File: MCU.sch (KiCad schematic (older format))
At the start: 4 parts

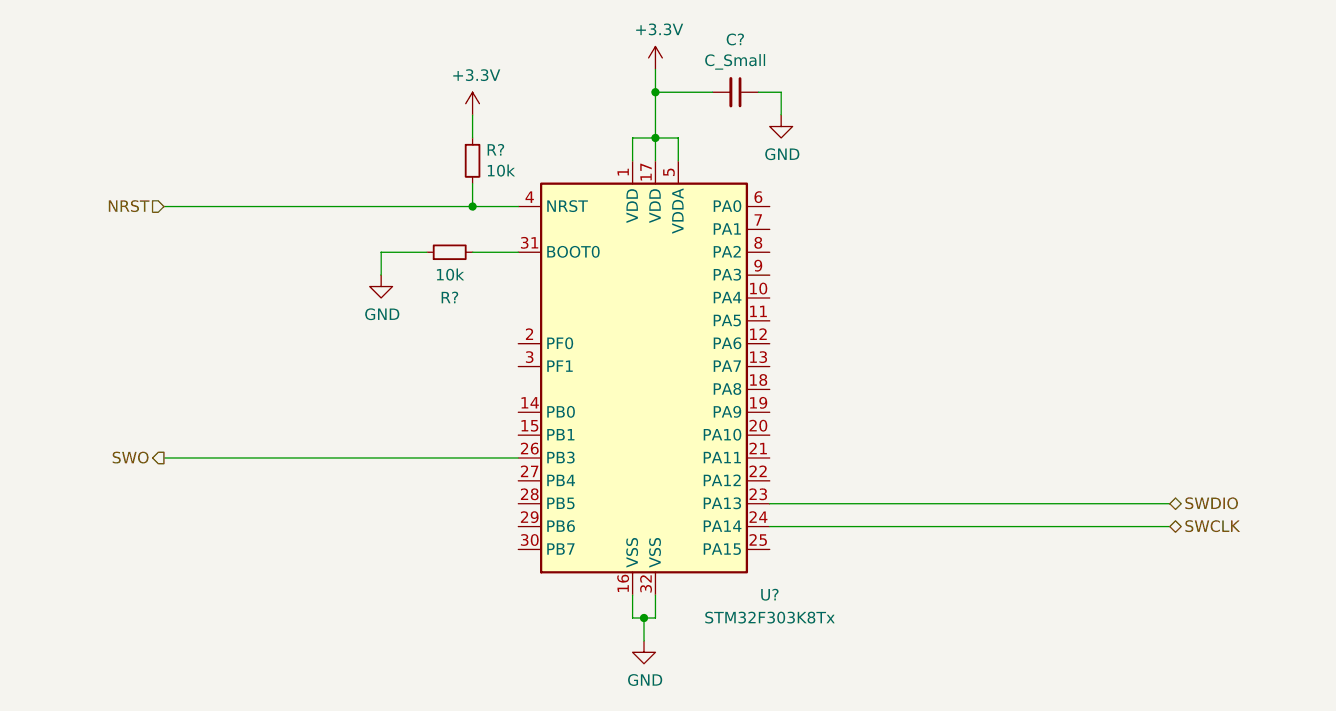
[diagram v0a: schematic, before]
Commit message: デッドタイム挿入回路を削除、マイコンブロック作成
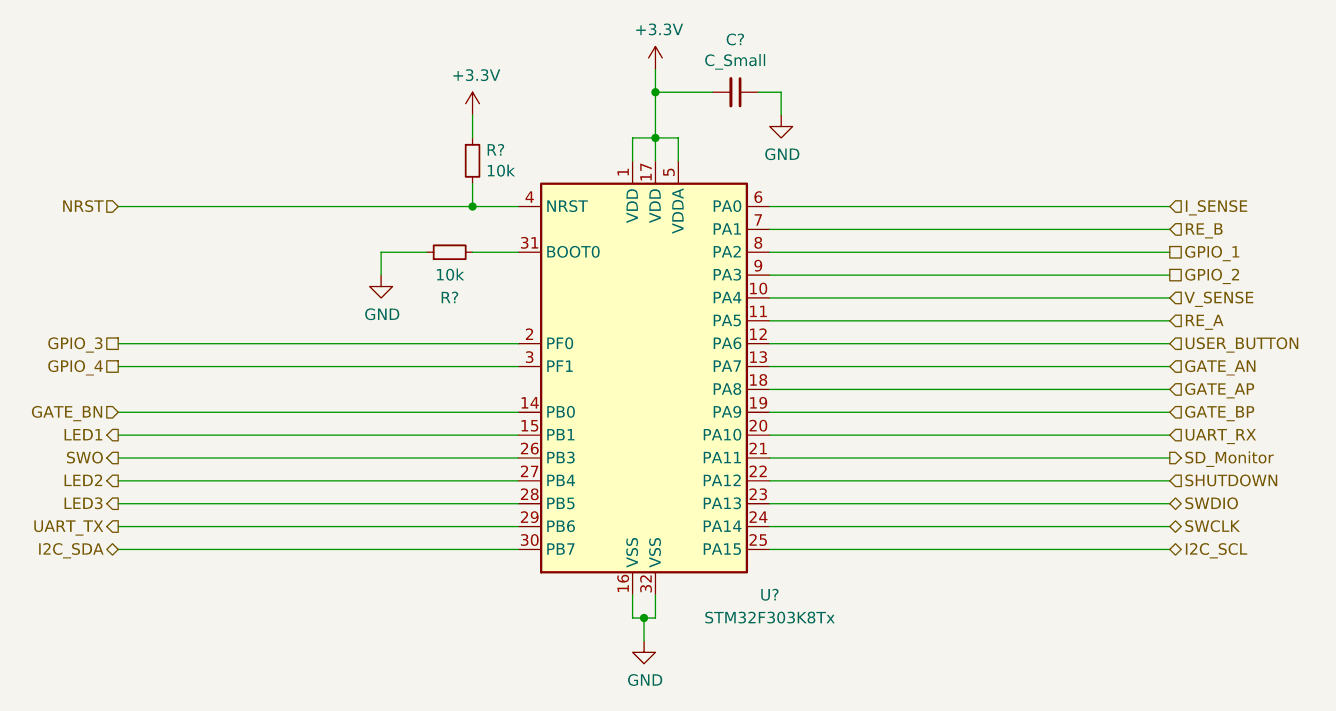
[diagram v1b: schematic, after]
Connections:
- net V_SENSE: now reaches U?.10 (PA4)
- net RE_A: now reaches U?.11 (PA5)
- net USER_BUTTON: now reaches U?.12 (PA6)
- net GATE_AN: now reaches U?.13 (PA7)
- net GATE_BN: now reaches U?.14 (PB0)
- net LED1: now reaches U?.15 (PB1)
- net GATE_AP: now reaches U?.18 (PA8)
- net GATE_BP: now reaches U?.19 (PA9)
- net GPIO_3: now reaches U?.2 (PF0)
- net UART_RX: now reaches U?.20 (PA10)
- net SD_Monitor: now reaches U?.21 (PA11)
- net SHUTDOWN: now reaches U?.22 (PA12)
- net I2C_SCL: now reaches U?.25 (PA15)
- net LED2: now reaches U?.27 (PB4)
- net LED3: now reaches U?.28 (PB5)
- net UART_TX: now reaches U?.29 (PB6)
- net GPIO_4: now reaches U?.3 (PF1)
- net I2C_SDA: now reaches U?.30 (PB7)
- net I_SENSE: now reaches U?.6 (PA0)
- net RE_B: now reaches U?.7 (PA1)
- net GPIO_1: now reaches U?.8 (PA2)
- net GPIO_2: now reaches U?.9 (PA3)
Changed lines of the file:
@@
 Wire Wire Line
 	5000 2750 5000 2850
-Text HLabel 3650 3150 0    50   Input ~ 0
+Text HLabel 3450 3150 0    50   Input ~ 0
 NRST
 Wire Wire Line
-	3650 3150 5000 3150
+	3450 3150 5000 3150
 Connection ~ 5000 3150
 $Comp
@@
 	6300 4550 8050 4550
 Wire Wire Line
-	5200 4250 3650 4250
-Text HLabel 3650 4250 0    50   Output ~ 0
+	5200 4250 3450 4250
+Text HLabel 3450 4250 0    50   Output ~ 0
 SWO
+Text HLabel 8050 3150 2    50   Input ~ 0
+I_SENSE
+Text HLabel 8050 3550 2    50   Input ~ 0
+V_SENSE
+Wire Wire Line
+	6300 3150 8050 3150
+Wire Wire Line
+	8050 3550 6300 3550
+Wire Wire Line
+	6300 3950 8050 3950
+Text HLabel 8050 3950 2    50   Input ~ 0
+GATE_AP
+Text HLabel 8050 3850 2    50   Input ~ 0
+GATE_AN
+Wire Wire Line
+	8050 3850 6300 3850
+Text HLabel 8050 4050 2    50   Input ~ 0
+GATE_BP
+Wire Wire Line
+	8050 4050 6300 4050
+Wire Wire Line
+	5200 4050 3450 4050
+Text HLabel 3450 4050 0    50   Input ~ 0
+GATE_BN
+Text HLabel 3450 4550 0    50   Output ~ 0
+UART_TX
+Wire Wire Line
+	3450 4550 5200 4550
+Text HLabel 8050 4150 2    50   Input ~ 0
+UART_RX
+Wire Wire Line
+	6300 4150 8050 4150
+Wire Wire Line
+	5200 4650 3450 4650
+Text HLabel 3450 4650 0    50   BiDi ~ 0
+I2C_SDA
+Text HLabel 8050 4650 2    50   BiDi ~ 0
+I2C_SCL
+Wire Wire Line
+	8050 4650 6300 4650
+Text HLabel 8050 3650 2    50   Input ~ 0
+RE_A
+Wire Wire Line
+	8050 3650 6300 3650
+Text HLabel 8050 3250 2    50   Input ~ 0
+RE_B
+Wire Wire Line
+	8050 3250 6300 3250
+Text HLabel 3450 4150 0    50   Output ~ 0
+LED1
+Text HLabel 3450 4350 0    50   Output ~ 0
+LED2
+Text HLabel 3450 4450 0    50   Output ~ 0
+LED3
+Wire Wire Line
+	3450 4150 5200 4150
+Wire Wire Line
+	5200 4350 3450 4350
+Wire Wire Line
+	3450 4450 5200 4450
+Text HLabel 8050 3750 2    50   Input ~ 0
+USER_BUTTON
+Wire Wire Line
+	8050 3750 6300 3750
+Text HLabel 8050 4250 2    50   Output ~ 0
+SD_Monitor
+Text HLabel 8050 4350 2    50   Input ~ 0
+SHUTDOWN
+Wire Wire Line
+	6300 4250 8050 4250
+Wire Wire Line
+	6300 4350 8050 4350
+Text HLabel 8050 3350 2    50   UnSpc ~ 0
+GPIO_1
+Text HLabel 8050 3450 2    50   UnSpc ~ 0
+GPIO_2
+Text HLabel 3450 3750 0    50   UnSpc ~ 0
+GPIO_3
+Text HLabel 3450 3850 0    50   UnSpc ~ 0
+GPIO_4
+Wire Wire Line
+	3450 3750 5200 3750
+Wire Wire Line
+	5200 3850 3450 3850
+Wire Wire Line
+	8050 3350 6300 3350
+Wire Wire Line
+	6300 3450 8050 3450
 $EndSCHEMATC

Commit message: 第１版回路図完成
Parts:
- C12: renamed from C?; value C_Small -> 0.1u
- gave numbers to parts that had none: 3
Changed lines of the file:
@@
 encoding utf-8
 Sheet 2 5
-Title ""
+Title "MCU"
 Date ""
 Rev ""
@@
 $EndDescr
 $Comp
-L MCU_ST_STM32F3:STM32F303K8Tx U?
+L MCU_ST_STM32F3:STM32F303K8Tx U4
 U 1 1 5C7B8CAF
 P 5800 3850
-F 0 "U?" H 6300 2850 50  0000 C CNN
+F 0 "U4" H 6300 2850 50  0000 C CNN
 F 1 "STM32F303K8Tx" H 6300 2750 50  0000 C CNN
 F 2 "Package_QFP:LQFP-32_7x7mm_P0.8mm" H 5300 2950 50  0001 R CNN
@@
 $EndComp
 $Comp
-L power:GND #PWR?
+L power:GND #PWR033
 U 1 1 5C94C9F7
 P 5750 5050
-F 0 "#PWR?" H 5750 4800 50  0001 C CNN
+F 0 "#PWR033" H 5750 4800 50  0001 C CNN
 F 1 "GND" H 5755 4877 50  0000 C CNN
 F 2 "" H 5750 5050 50  0001 C CNN
@@
 Connection ~ 5800 2850
 $Comp
-L power:+3.3V #PWR?
+L power:+3.3V #PWR034
 U 1 1 5C94CACA
 P 5800 2550
-F 0 "#PWR?" H 5800 2400 50  0001 C CNN
+F 0 "#PWR034" H 5800 2400 50  0001 C CNN
 F 1 "+3.3V" H 5815 2723 50  0000 C CNN
 F 2 "" H 5800 2550 50  0001 C CNN
@@
 	5800 2550 5800 2650
 $Comp
-L Device:C_Small C?
+L Device:C_Small C12
 U 1 1 5C94CBDE
 P 6150 2650
-F 0 "C?" V 5921 2650 50  0000 C CNN
-F 1 "C_Small" V 6012 2650 50  0000 C CNN
+F 0 "C12" V 5921 2650 50  0000 C CNN
+F 1 "0.1u" V 6012 2650 50  0000 C CNN
 F 2 "" H 6150 2650 50  0001 C CNN
 F 3 "~" H 6150 2650 50  0001 C CNN
@@
 	6350 2650 6350 2750
 $Comp
-L power:GND #PWR?
+L power:GND #PWR035
 U 1 1 5C94CD56
 P 6350 2750
-F 0 "#PWR?" H 6350 2500 50  0001 C CNN
+F 0 "#PWR035" H 6350 2500 50  0001 C CNN
 F 1 "GND" H 6355 2577 50  0000 C CNN
 F 2 "" H 6350 2750 50  0001 C CNN
@@
 $EndComp
 $Comp
-L Device:R_Small R?
+L Device:R_Small R12
 U 1 1 5C94D649
 P 5000 2950
-F 0 "R?" H 5059 2996 50  0000 L CNN
+F 0 "R12" H 5059 2996 50  0000 L CNN
 F 1 "10k" H 5059 2905 50  0000 L CNN
 F 2 "" H 5000 2950 50  0001 C CNN
@@
 	5000 3150 5000 3050
 $Comp
-L power:+3.3V #PWR?
+L power:+3.3V #PWR032
 U 1 1 5C94D8DA
 P 5000 2750
-F 0 "#PWR?" H 5000 2600 50  0001 C CNN
+F 0 "#PWR032" H 5000 2600 50  0001 C CNN
 F 1 "+3.3V" H 5015 2923 50  0000 C CNN
 F 2 "" H 5000 2750 50  0001 C CNN
@@
 Connection ~ 5000 3150
 $Comp
-L Device:R_Small R?
+L Device:R_Small R11
 U 1 1 5C94DBF8
 P 4900 3350
-F 0 "R?" V 4700 3350 50  0000 C CNN
+F 0 "R11" V 4700 3350 50  0000 C CNN
 F 1 "10k" V 4800 3350 50  0000 C CNN
 F 2 "" H 4900 3350 50  0001 C CNN
@@
 	4800 3350 4600 3350
 $Comp
-L power:GND #PWR?
+L power:GND #PWR031
 U 1 1 5C94E043
 P 4600 3450
-F 0 "#PWR?" H 4600 3200 50  0001 C CNN
+F 0 "#PWR031" H 4600 3200 50  0001 C CNN
 F 1 "GND" H 4605 3277 50  0000 C CNN
 F 2 "" H 4600 3450 50  0001 C CNN

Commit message: フットプリント割り付け＆Netリスト出力
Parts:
- C12: footprint (none) -> Capacitors_SMD:C_0603_HandSoldering
- R11, R12: footprint (none) -> Resistors_SMD:R_0603_HandSoldering
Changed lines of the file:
@@
 F 0 "C12" V 5921 2650 50  0000 C CNN
 F 1 "0.1u" V 6012 2650 50  0000 C CNN
-F 2 "" H 6150 2650 50  0001 C CNN
+F 2 "Capacitors_SMD:C_0603_HandSoldering" H 6150 2650 50  0001 C CNN
 F 3 "~" H 6150 2650 50  0001 C CNN
 	1    6150 2650
@@
 F 0 "R12" H 5059 2996 50  0000 L CNN
 F 1 "10k" H 5059 2905 50  0000 L CNN
-F 2 "" H 5000 2950 50  0001 C CNN
+F 2 "Resistors_SMD:R_0603_HandSoldering" H 5000 2950 50  0001 C CNN
 F 3 "~" H 5000 2950 50  0001 C CNN
 	1    5000 2950
@@
 F 0 "R11" V 4700 3350 50  0000 C CNN
 F 1 "10k" V 4800 3350 50  0000 C CNN
-F 2 "" H 4900 3350 50  0001 C CNN
+F 2 "Resistors_SMD:R_0603_HandSoldering" H 4900 3350 50  0001 C CNN
 F 3 "~" H 4900 3350 50  0001 C CNN
 	1    4900 3350

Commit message: STM32のふっとプリント割り付け修正
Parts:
- U4: footprint Package_QFP:LQFP-32_7x7mm_P0.8mm -> Housings_QFP:LQFP-32_7x7mm_Pitch0.8mm
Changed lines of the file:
@@
 F 0 "U4" H 6300 2850 50  0000 C CNN
 F 1 "STM32F303K8Tx" H 6300 2750 50  0000 C CNN
-F 2 "Package_QFP:LQFP-32_7x7mm_P0.8mm" H 5300 2950 50  0001 R CNN
+F 2 "Housings_QFP:LQFP-32_7x7mm_Pitch0.8mm" H 5300 2950 50  0001 R CNN
 F 3 "http://www.st.com/st-web-ui/static/active/en/resource/technical/document/datasheet/DM00092070.pdf" H 5800 3850 50  0001 C CNN
 	1    5800 3850
